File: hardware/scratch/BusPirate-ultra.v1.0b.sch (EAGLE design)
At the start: 165 parts, among them IC1 23LC1024, IC10 SN74LVC1T45DBV, IC11 SN74LVC1T45DBV, IC12 74LVC1G07DBV, IC13 SN74LVC1T45DBV, IC17 74LVC1G07DBV, IC18 SN74LVC1T45DBV, IC19 74LVC1G07DBV, IC2 23LC1024, IC20 SN74LVC1T45DBV, IC21 74LVC1G07DBV, IC22 SN74LVC1T45DBV, IC23 MCP1824_ADJ, IC24 74HCT4051, IC4 74LVC1G07DBV, IC5 74LVC1G07DBV, IC6 74LVC1G07DBV, IC7 74LVC1G07DBV, IC8 SN74LVC1T45DBV, IC9 SN74LVC1T45DBV, J2 CON_HEADER_1X04, J4 CON_HEADER_1X10-RIGHT_ANGLED_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, Q1 DMMT3906W, U1 W25X40CL, U2 STM32F103ZX, U3 ICE40HX4K, U4 MCP6001, U5 74LVC245A, U7 MCP6001, U8 74HCT4066PW, U9 74HCT4066PW

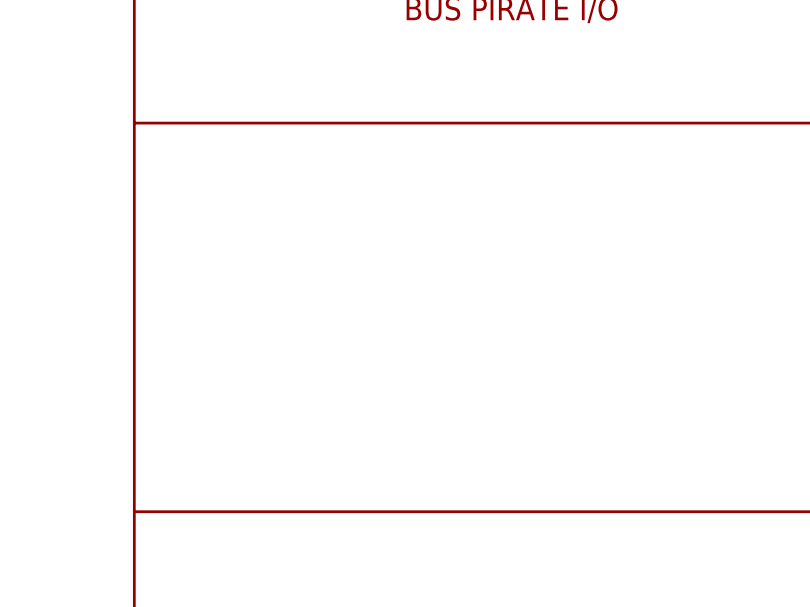
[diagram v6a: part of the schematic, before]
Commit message: added 10pin header for display
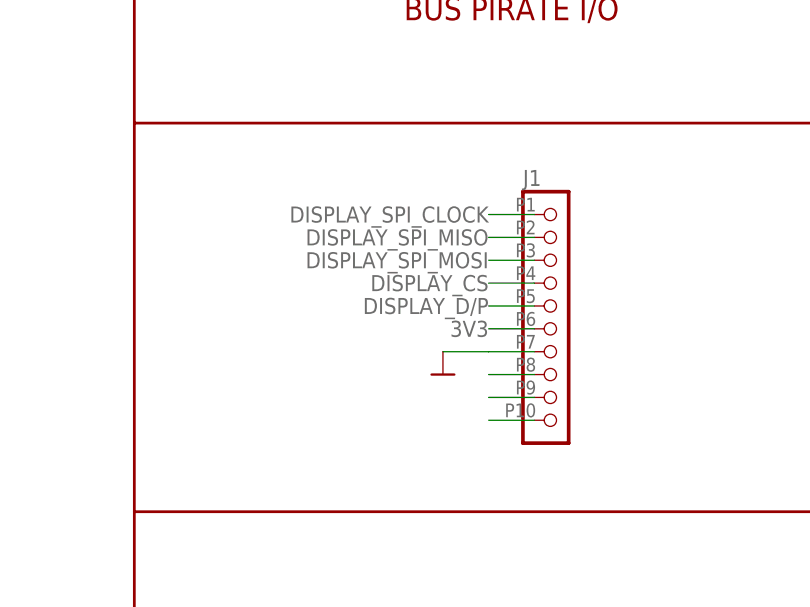
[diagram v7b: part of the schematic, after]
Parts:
- added J1: CON_MOLEX_MALE_SMT_SH_1.25, dp_devices.v6:CON_MOLEX_MALE_SMT_SH_1.25
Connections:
- new net DISPLAY_CS: J1.4
- new net DISPLAY_D/P: J1.5
- new net N$62: J1.8
- new net N$63: J1.9
- new net N$66: J1.10
- net 3V3: now also J1.6
- net DISPLAY_SPI_CLOCK: now also J1.1
- net DISPLAY_SPI_MISO: now also J1.2
- net DISPLAY_SPI_MOSI: now also J1.3
- net GND: now also J1.7
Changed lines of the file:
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@@
 <part name="U5" library="dp_devices.v6" deviceset="IC_BUFF_74LVC245A" device="-TSSOP20" value="74LVC245A"/>
 <part name="GND82" library="dp_devices.v6" deviceset="SUPPLY_GND" device=""/>
+<part name="J1" library="dp_devices.v6" deviceset="CON_MOLEX_MALE_SMT_SH_1.25" device=""/>
+<part name="GND69" library="dp_devices.v6" deviceset="SUPPLY_GND" device=""/>
 </parts>
 <sheets>
@@
 <instance part="GND82" gate="G$1" x="314.96" y="78.74" smashed="yes"/>
 <instance part="U5" gate="SUPPLY" x="505.46" y="330.2"/>
+<instance part="J1" gate="J" x="711.2" y="55.88"/>
+<instance part="GND69" gate="G$1" x="701.04" y="50.8" smashed="yes"/>
 </instances>
 <busses>
@@
 <junction x="314.96" y="81.28"/>
 </segment>
+<segment>
+<pinref part="J1" gate="J" pin="7"/>
+<wire x1="711.2" y1="53.34" x2="706.12" y2="53.34" width="0.1524" layer="91"/>
+<pinref part="GND69" gate="G$1" pin="GND"/>
+<wire x1="706.12" y1="53.34" x2="701.04" y2="53.34" width="0.1524" layer="91"/>
+</segment>
 </net>
 <net name="3V3" class="0">
@@
 <label x="513.08" y="299.72" size="1.778" layer="95"/>
 </segment>
+<segment>
+<pinref part="J1" gate="J" pin="6"/>
+<wire x1="711.2" y1="55.88" x2="706.12" y2="55.88" width="0.1524" layer="91"/>
+<label x="706.12" y="55.88" size="1.778" layer="95" align="center-right"/>
+</segment>
 </net>
 <net name="N$7" class="0">
@@
 <label x="35.56" y="416.56" size="1.778" layer="95" align="center-right"/>
 </segment>
+<segment>
+<pinref part="J1" gate="J" pin="1"/>
+<wire x1="711.2" y1="68.58" x2="706.12" y2="68.58" width="0.1524" layer="91"/>
+<label x="706.12" y="68.58" size="1.778" layer="95" align="center-right"/>
+</segment>
 </net>
 <net name="DISPLAY_SPI_MOSI" class="0">
@@
 <label x="35.56" y="411.48" size="1.778" layer="95" align="center-right"/>
 </segment>
+<segment>
+<pinref part="J1" gate="J" pin="3"/>
+<wire x1="711.2" y1="63.5" x2="706.12" y2="63.5" width="0.1524" layer="91"/>
+<label x="706.12" y="63.5" size="1.778" layer="95" align="center-right"/>
+</segment>
 </net>
 <net name="DISPLAY_SPI_MISO" class="0">
@@
 <label x="35.56" y="414.02" size="1.778" layer="95" align="center-right"/>
 </segment>
+<segment>
+<pinref part="J1" gate="J" pin="2"/>
+<wire x1="711.2" y1="66.04" x2="706.12" y2="66.04" width="0.1524" layer="91"/>
+<label x="706.12" y="66.04" size="1.778" layer="95" align="center-right"/>
+</segment>
 </net>
 <net name="N$3" class="0">
@@
 </segment>
 </net>
+<net name="DISPLAY_CS" class="0">
+<segment>
+<pinref part="J1" gate="J" pin="4"/>
+<wire x1="711.2" y1="60.96" x2="706.12" y2="60.96" width="0.1524" layer="91"/>
+<label x="706.12" y="60.96" size="1.778" layer="95" align="center-right"/>
+</segment>
+</net>
+<net name="DISPLAY_D/P" class="0">
+<segment>
+<pinref part="J1" gate="J" pin="5"/>
+<wire x1="711.2" y1="58.42" x2="706.12" y2="58.42" width="0.1524" layer="91"/>
+<label x="706.12" y="58.42" size="1.778" layer="95" align="center-right"/>
+</segment>
+</net>
+<net name="N$62" class="0">
+<segment>
+<pinref part="J1" gate="J" pin="8"/>
+<wire x1="711.2" y1="50.8" x2="706.12" y2="50.8" width="0.1524" layer="91"/>
+</segment>
+</net>
+<net name="N$63" class="0">
+<segment>
+<pinref part="J1" gate="J" pin="9"/>
+<wire x1="711.2" y1="48.26" x2="706.12" y2="48.26" width="0.1524" layer="91"/>
+</segment>
+</net>
+<net name="N$66" class="0">
+<segment>
+<pinref part="J1" gate="J" pin="10"/>
+<wire x1="711.2" y1="45.72" x2="706.12" y2="45.72" width="0.1524" layer="91"/>
+</segment>
+</net>
